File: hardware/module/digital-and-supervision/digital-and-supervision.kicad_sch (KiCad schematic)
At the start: 8 parts

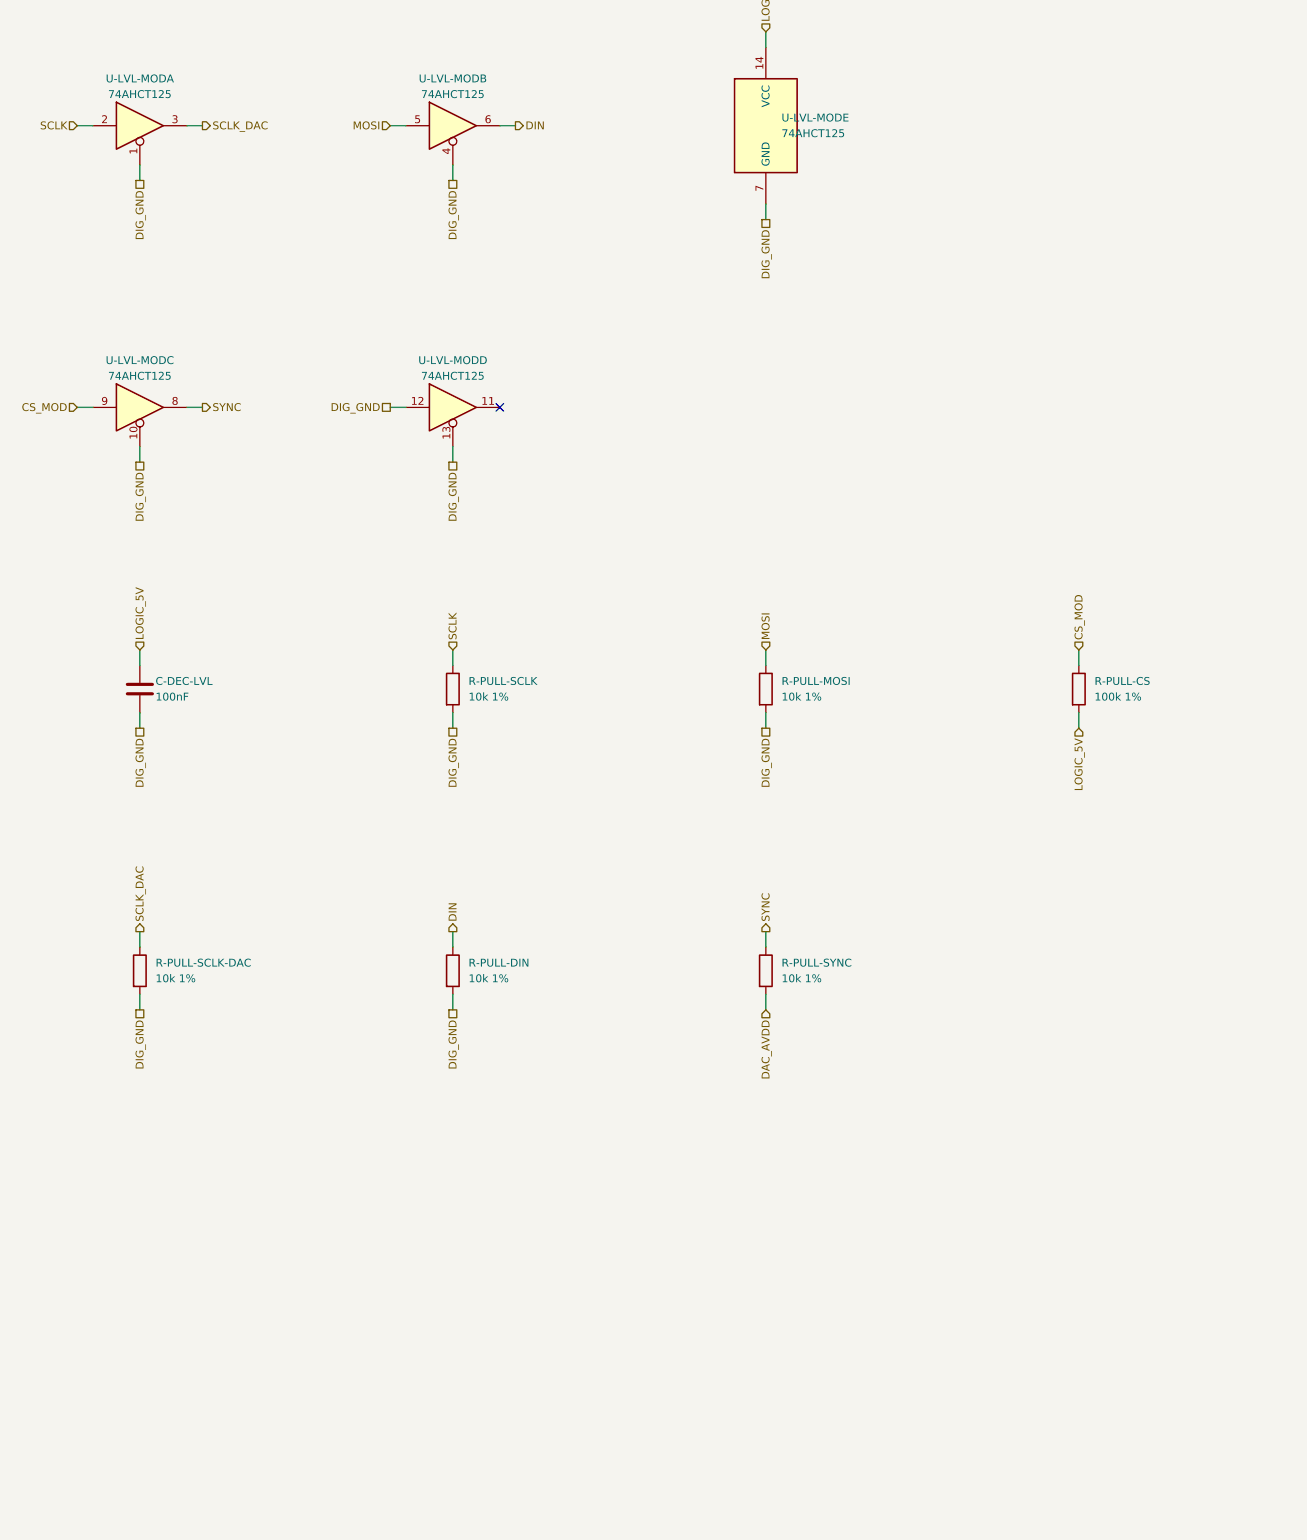
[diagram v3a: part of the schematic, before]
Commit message: WIP SPI link: U-TVS-SPI to the pad side, R-SPI-SER 82R; module receiver U-RX-MOD (74AHCT14) behind R-RX-MOD/C-RX-MOD
Co-Authored-By: Claude Opus 5.5 <noreply@anthropic.com>
Claude-Session: https://claude.ai/code/session_01LmB4muFXnoLprWX4JzuJ5A
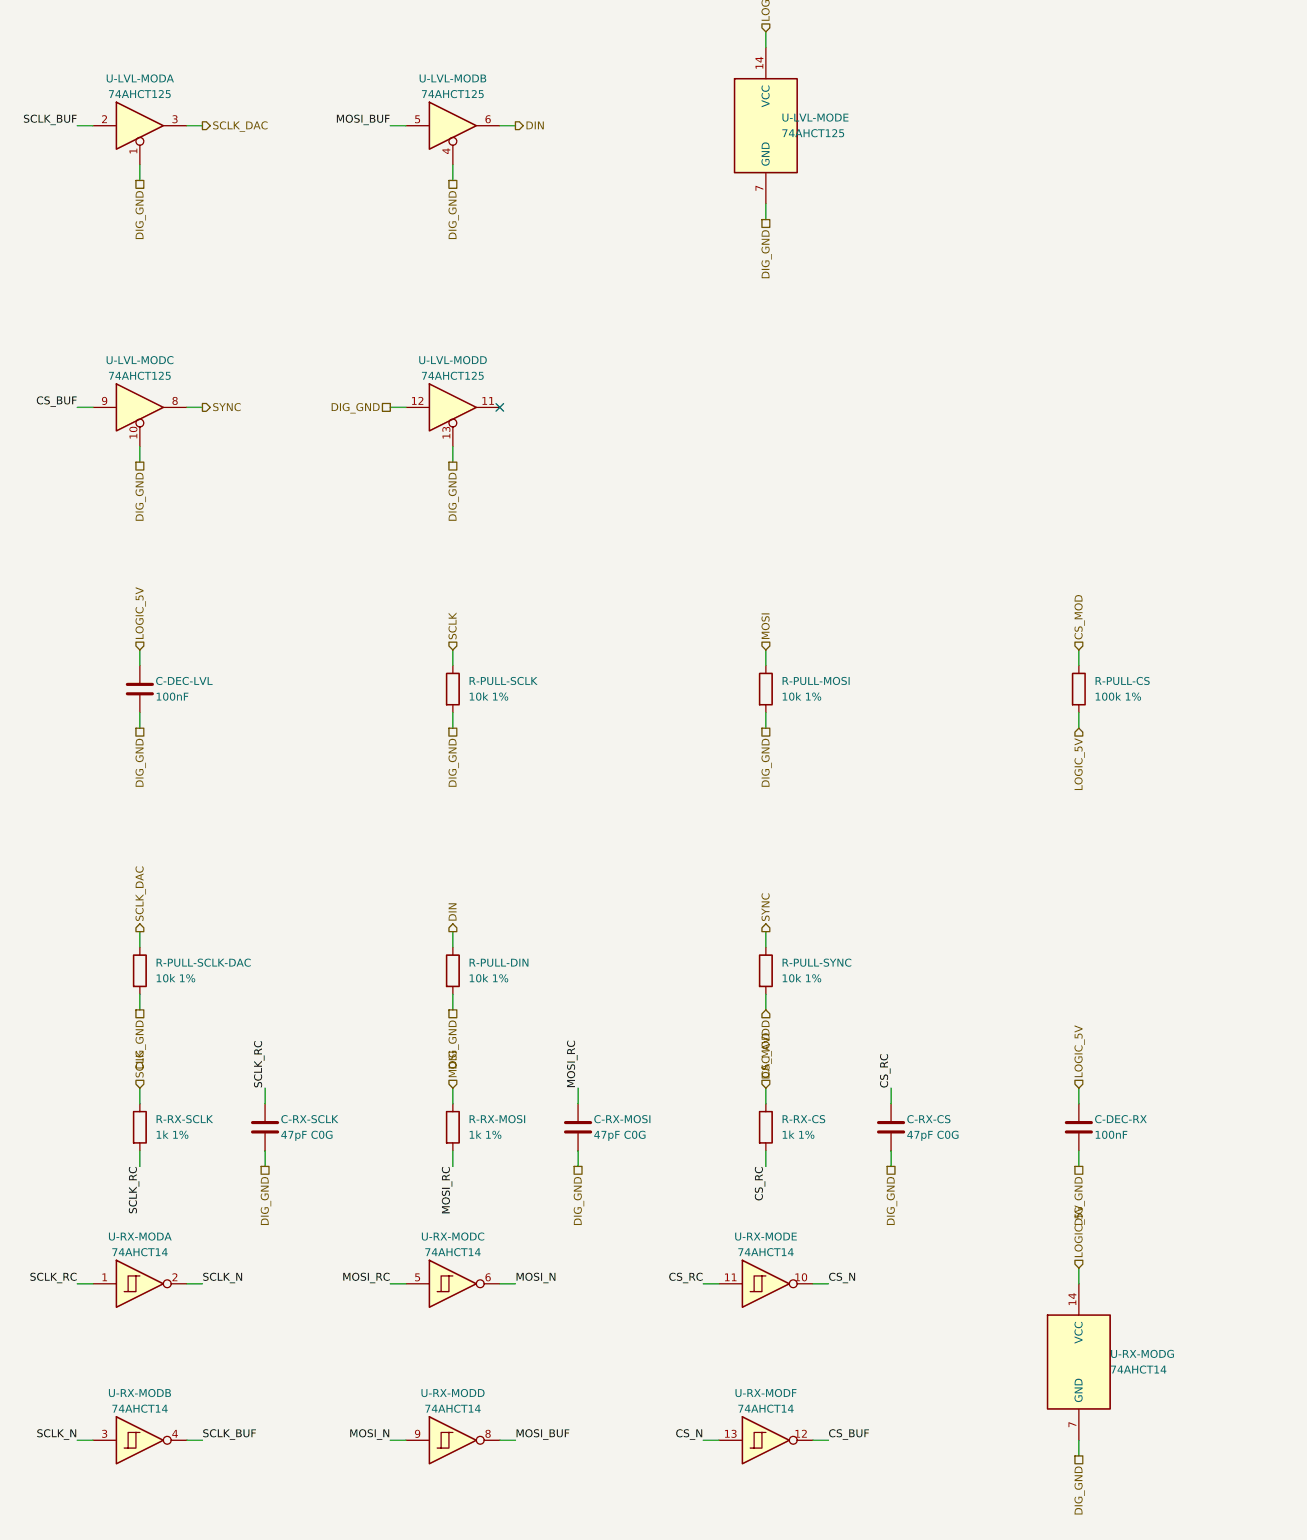
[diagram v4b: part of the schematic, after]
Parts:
- added C-DEC-RX: 100nF, Capacitor_SMD:C_0805_2012Metric, symbol Device:C
- added C-RX-CS, C-RX-MOSI, C-RX-SCLK: 47pF C0G, Capacitor_SMD:C_0805_2012Metric, symbol Device:C
- added R-RX-CS, R-RX-MOSI, R-RX-SCLK: 1k 1%, Resistor_SMD:R_0805_2012Metric, symbol Device:R
- added U-RX-MOD: 74AHCT14, Package_SO:SOIC-14_3.9x8.7mm_P1.27mm, symbol 74xx:74HC14
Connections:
- net CS_MOD: now also R-RX-CS.1; no longer U-LVL-MOD.9
- net DIG_GND: now also C-DEC-RX.2, C-RX-CS.2, C-RX-MOSI.2, C-RX-SCLK.2, U-RX-MOD.7 (GND)
- net LOGIC_5V: now also C-DEC-RX.1, U-RX-MOD.14 (VCC)
- net MOSI: now also R-RX-MOSI.1; no longer U-LVL-MOD.5
- net SCLK: now also R-RX-SCLK.1; no longer U-LVL-MOD.2
- new net CS_BUF: U-LVL-MOD.9, U-RX-MOD.12
- new net CS_N: U-RX-MOD.10, U-RX-MOD.13
- new net CS_RC: C-RX-CS.1, R-RX-CS.2, U-RX-MOD.11
- new net MOSI_BUF: U-LVL-MOD.5, U-RX-MOD.8
- new net MOSI_N: U-RX-MOD.6, U-RX-MOD.9
- new net MOSI_RC: C-RX-MOSI.1, R-RX-MOSI.2, U-RX-MOD.5
- new net SCLK_BUF: U-LVL-MOD.2, U-RX-MOD.4
- new net SCLK_N: U-RX-MOD.2, U-RX-MOD.3
- new net SCLK_RC: C-RX-SCLK.1, R-RX-SCLK.2, U-RX-MOD.1

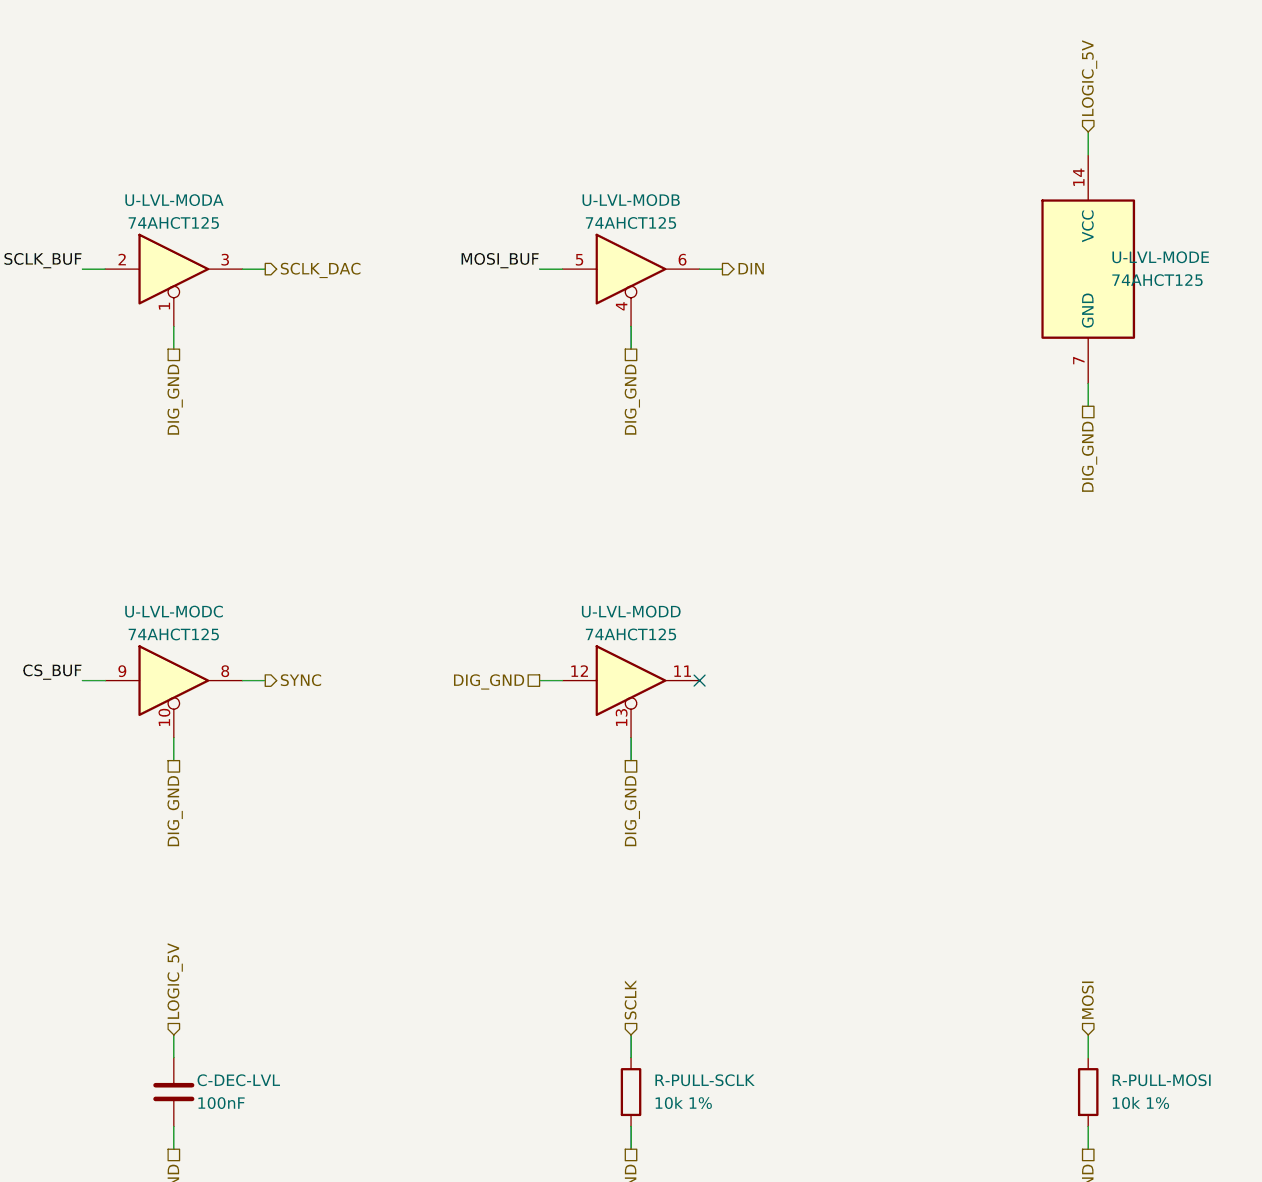
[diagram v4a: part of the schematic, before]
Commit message: U-LVL-MOD on DAC_AVDD (owner, option 1); LM317L divider values to their positions
The 74AHCT125 driving the DAC8568's SYNC/SCLK/DIN now takes its VCC (and
C-DEC-LVL) from DAC_AVDD, so its outputs can never sit over the DAC's
AVDD + 0.3 V absolute maximum while the two 5 V rails disagree.

R-REG-SET-HI (ADJ to OUT) and R-REG-SET-LO (ADJ to GND) carried each
other's values: as netlisted the LM317L set 1.25 x (1 + 150/475) = 1.65 V,
not dac-rail's 1.25 x (1 + 475/150). The sims had swapped the names back
silently. Values, MPN and LCSC swapped on the sheet and in the fragment.

Co-Authored-By: Claude Opus 5.5 <noreply@anthropic.com>
Claude-Session: https://claude.ai/code/session_01LmB4muFXnoLprWX4JzuJ5A
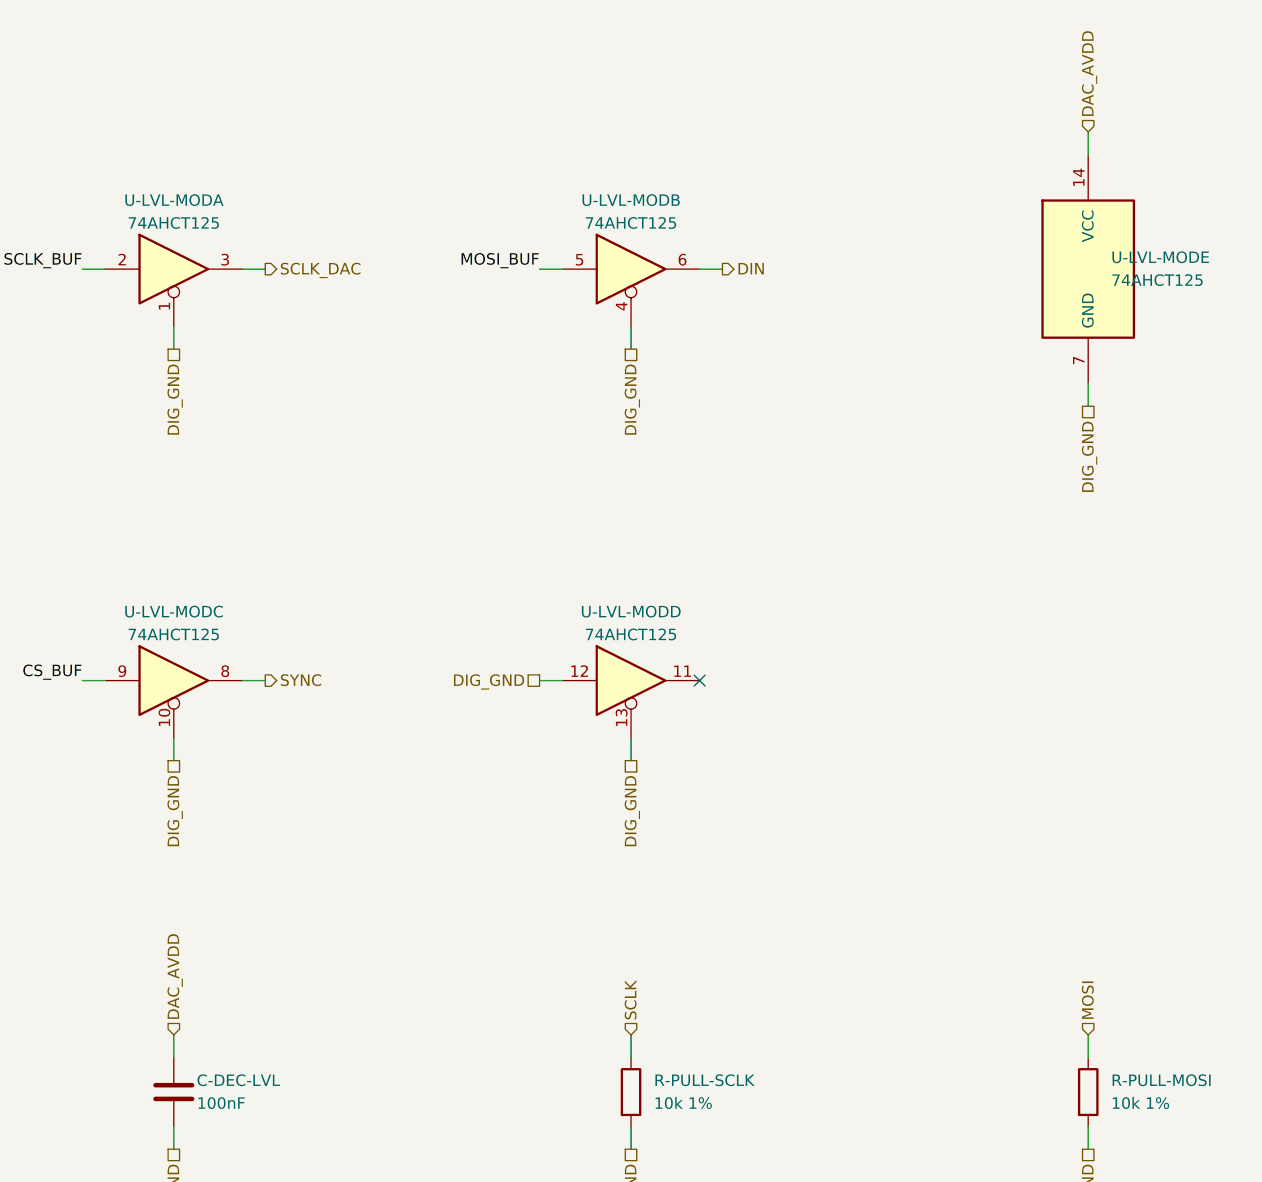
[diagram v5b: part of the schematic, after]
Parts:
- C-DEC-LVL: Note VCC to DIG_GND, at the pin -> U-LVL-MOD's VCC (DAC_AVDD) to DIG_GND, at the pin
- U-LVL-MOD: Note OE IS TIED ENABLED AND MUST STAY THAT WAY - the presence co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 -> VCC IS DAC_AVDD, NOT LOGIC_5V, AND MUST STAY THAT WAY (owne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
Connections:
- net DAC_AVDD: now also C-DEC-LVL.1, U-LVL-MOD.14 (VCC)
- net LOGIC_5V: no longer C-DEC-LVL.1, U-LVL-MOD.14 (VCC)

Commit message: DAC rail pages and sims: power-entry.md 'The DAC rail', dac8568, digital-and-supervision, breath pages, nets.yaml; module-own-draw ~32 mA; what-if power-off arm recorded
Co-Authored-By: Claude Opus 5.5 <noreply@anthropic.com>
Claude-Session: https://claude.ai/code/session_01LmB4muFXnoLprWX4JzuJ5A
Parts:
- R-PULL-SYNC: Note PULL-UP TO DAC_AVDD, the LM317's rail, NOT bus +5V: a pull-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 -> PULL-UP TO DAC_AVDD, U-REG-DAC's rail, NOT bus +5V: a pull-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
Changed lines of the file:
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@@
     (property "Row" "R-SPI-PULL" (at 142.24 187.96 0) (effects (font (size 1.27 1.27)) hide))
     (property "Pins" "1=1 2=2" (at 142.24 187.96 0) (effects (font (size 1.27 1.27)) hide))
-    (property "Note" "PULL-UP TO DAC_AVDD, the LM317's rail, NOT bus +5V: a pull-up belongs on its consumer's rail, and on the bus rail a reversed ribbon reaches the DAC's SYNC pin and turns a buffer failure into a DAC failure" (at 142.24 187.96 0) (effects (font (size 1.27 1.27)) hide))
+    (property "Note" "PULL-UP TO DAC_AVDD, U-REG-DAC's rail, NOT bus +5V: a pull-up belongs on its consumer's rail, and on the bus rail a reversed ribbon reaches the DAC's SYNC pin and turns a buffer failure into a DAC failure" (at 142.24 187.96 0) (effects (font (size 1.27 1.27)) hide))
     (property "Manufacturer" "UNI-ROYAL(Uniroyal Elec)" (at 142.24 187.96 0) (effects (font (size 1.27 1.27)) hide))
     (property "MPN" "0805W8F1002T5E" (at 142.24 187.96 0) (effects (font (size 1.27 1.27)) hide))
